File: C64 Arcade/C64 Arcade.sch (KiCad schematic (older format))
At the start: 53 parts, among them J1 Port_1, J10 P2_FIRE3, J11 P1_FIRE1, J12 P1_FIRE2, J13 P1_FIRE3, J14 PWR1, J15 PWR2, J2 Port_2, J3 DIR, J4 UP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

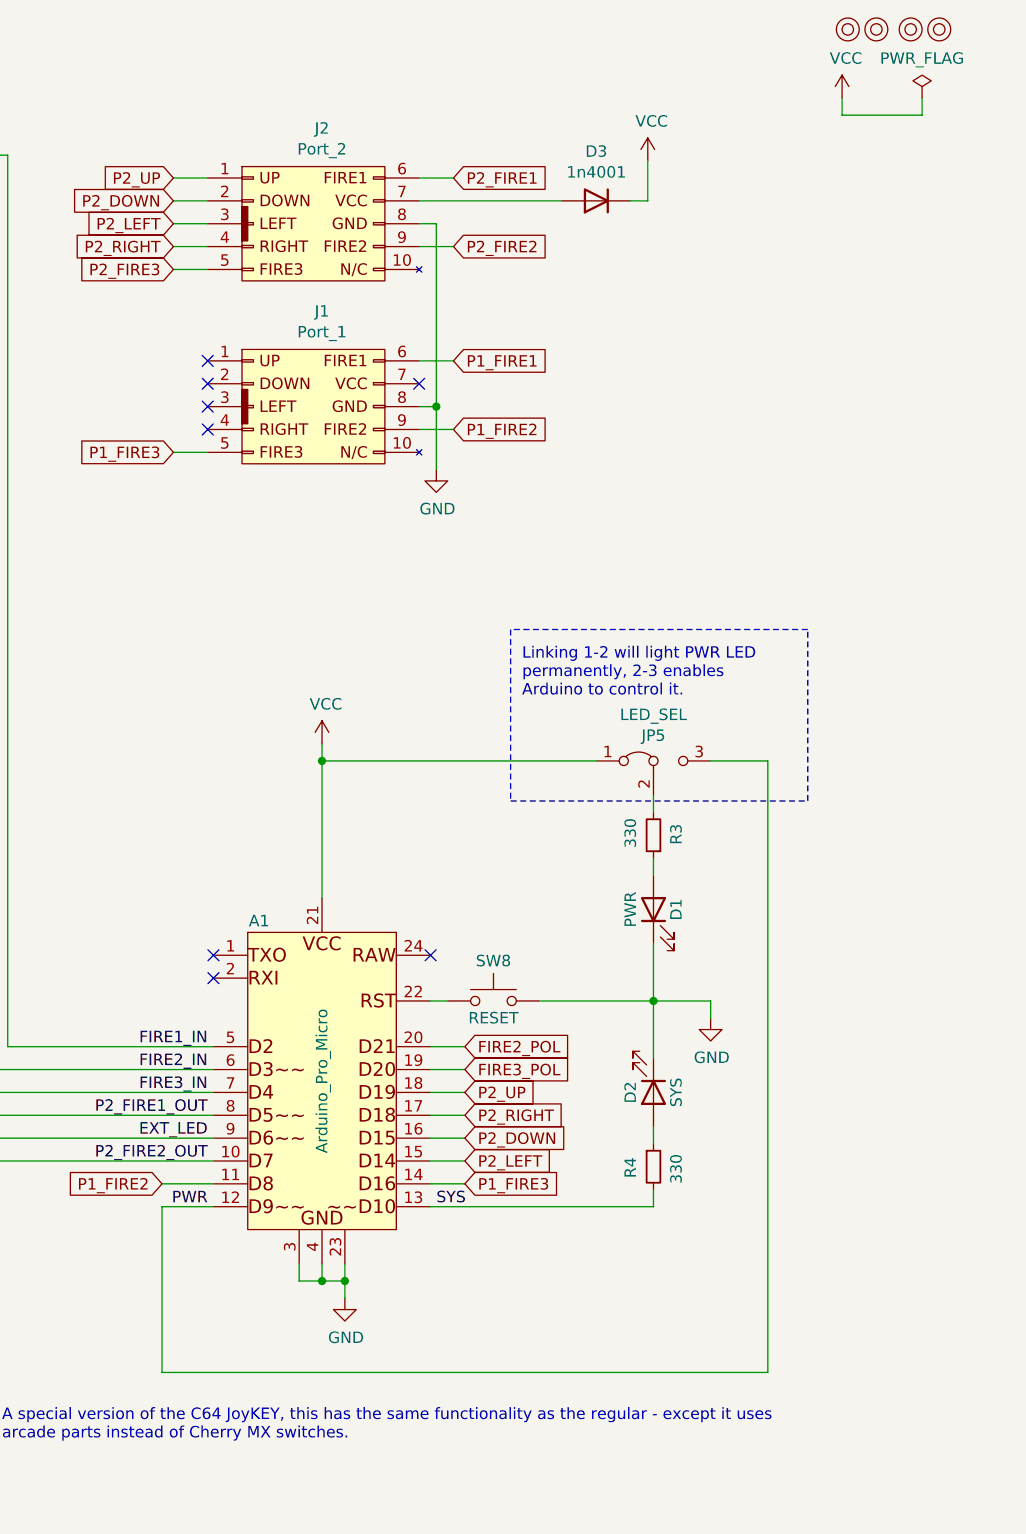
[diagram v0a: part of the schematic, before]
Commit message: Assigned arcade footprints
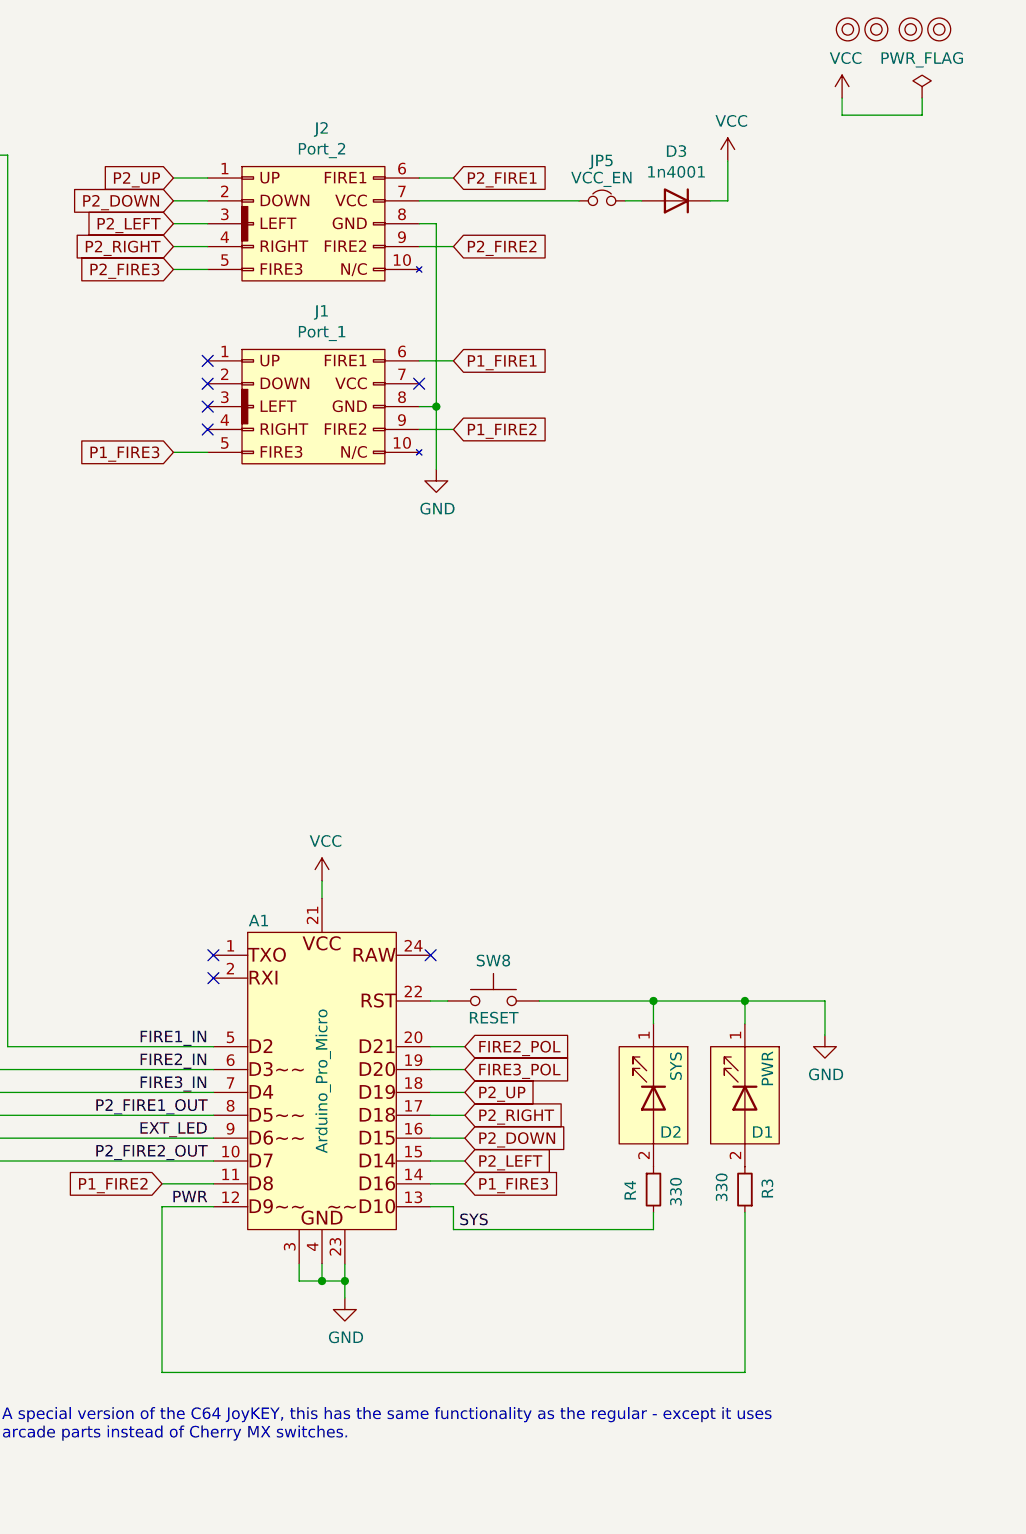
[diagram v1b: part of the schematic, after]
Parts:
- removed D1: PWR, LEDs:LED_D5.0mm, symbol Device:LED
- removed D2: SYS, LEDs:LED_D5.0mm, symbol Device:LED
- removed JP5: LED_SEL, solder_bridge:select, symbol Jumper:Jumper_3_Bridged12
- added D1: PWR, Connector_JST:JST_XH_B2B-XH-A_1x02_P2.50mm_Vertical, symbol arcade:LED_Plugin
- added D2: SYS, Connector_JST:JST_XH_B2B-XH-A_1x02_P2.50mm_Vertical, symbol arcade:LED_Plugin
- added JP5: VCC_EN, Connector_PinHeader_2.54mm:PinHeader_1x02_P2.54mm_Vertical, symbol Device:Jumper_NC_Small
- D10, D5, D6, D7, D8, D9, J10, J11, J12, J13, J14, J15, J4, J5, J6, J7, J8, J9: footprint (none) -> Connector_JST:JST_XH_B2B-XH-A_1x02_P2.50mm_Vertical
- J3: footprint (none) -> Connector_JST:JST_XH_B5B-XH-A_1x05_P2.50mm_Vertical
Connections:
- net GND: now also D1.1 (K), D2.1 (K)
- net PWR: now also R3.1
- net at J2.7 (Pin_7): now also JP5.1; no longer D3.2 (A)
- net at R3.2: now also D1.2 (A)
- net at R4.1: now also D2.2 (A)
- new net: D3.2 (A), JP5.2
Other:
- note removed: "Linking 1-2 will light PWR LED\npermanently, 2-3 enables\nArduino to control it."
- moved on the sheet: D3, R3, R4

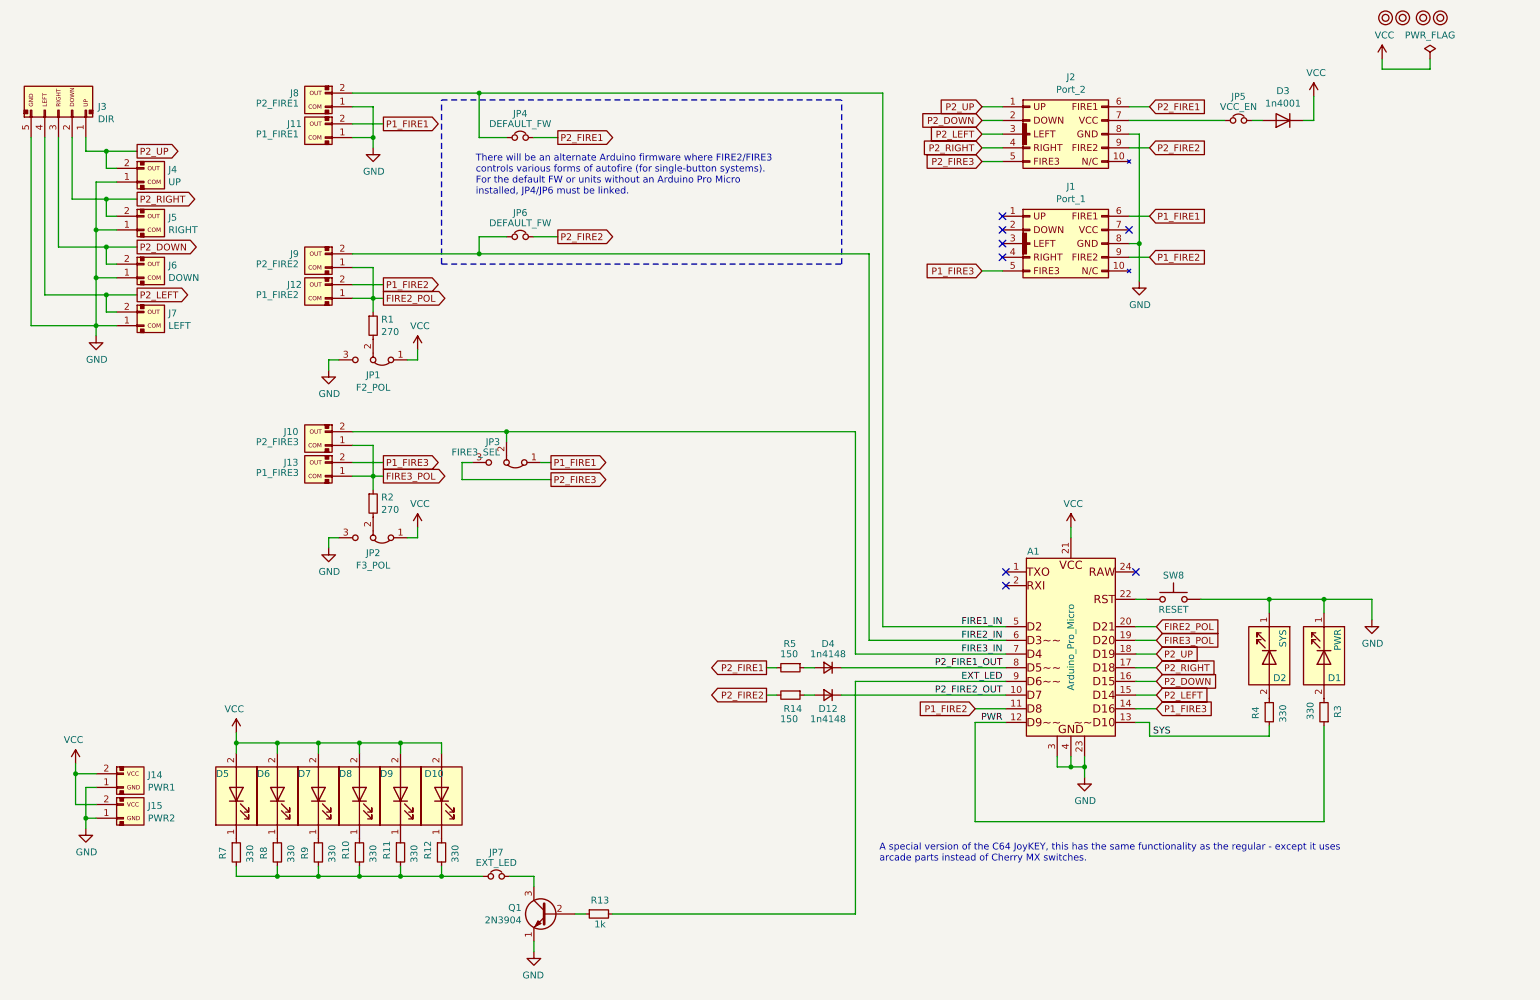
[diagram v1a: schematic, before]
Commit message: Arcade board layout done
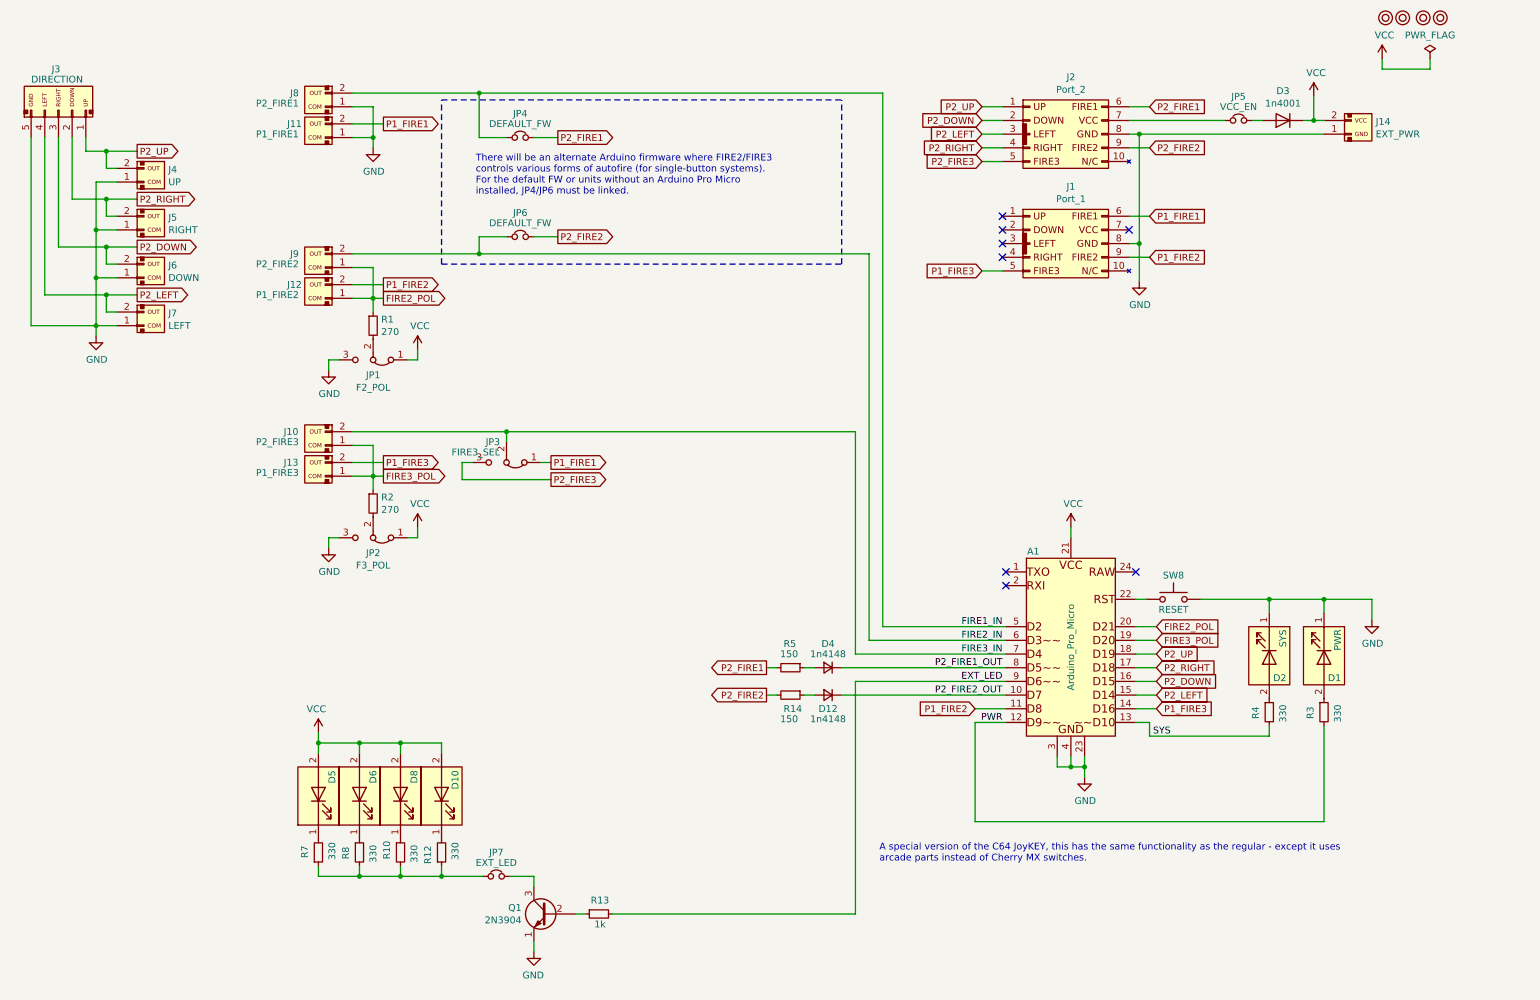
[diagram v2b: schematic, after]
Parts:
- removed D7, D9: LED_Plugin, Connector_JST:JST_XH_B2B-XH-A_1x02_P2.50mm_Vertical, symbol arcade:LED_Plugin
- removed J15: PWR2, Connector_JST:JST_XH_B2B-XH-A_1x02_P2.50mm_Vertical, symbol arcade:PWR
- removed R11, R9: 330, Resistor_THT:R_Axial_DIN0207_L6.3mm_D2.5mm_P10.16mm_Horizontal, symbol Device:R_Small
- J14: value PWR1 -> EXT_PWR
- J3: value DIR -> DIRECTION
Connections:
- net PWR: now also R3.2; no longer R3.1
- net at D1.2 (A): now also R3.1; no longer R3.2
- net at Q1.3 (C): now also JP7.1; no longer JP7.2
- net at D10.1 (K): now also R12.2; no longer R12.1
- net at R7.1: now also JP7.2, R10.2, R12.1, R8.2; no longer D5.1 (K)
- new net: D5.1 (K), R7.2
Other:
- moved on the sheet: D5, D6, D8, J14, R10, R7, R8
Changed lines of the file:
@@
 	3800 6750 3800 6825
 Wire Wire Line
-	3800 6825 3500 6825
-Wire Wire Line
 	3500 6750 3500 6825
-Connection ~ 3500 6825
-Wire Wire Line
-	3500 6825 3200 6825
 Wire Wire Line
 	3200 6750 3200 6825
-Connection ~ 3200 6825
 Wire Wire Line
 	3200 6825 2900 6825
 Wire Wire Line
 	2900 6750 2900 6825
-Connection ~ 2900 6825
-Wire Wire Line
-	2900 6825 2600 6825
-Wire Wire Line
-	2600 6750 2600 6825
-Connection ~ 2600 6825
-Wire Wire Line
-	2600 6825 2300 6825
-Wire Wire Line
-	2300 6750 2300 6825
-Connection ~ 3800 6825
 Wire Wire Line
 	3800 5925 3800 5850
 Wire Wire Line
-	3800 5850 3500 5850
-Wire Wire Line
 	3500 5850 3500 5925
 Wire Wire Line
-	3500 5850 3200 5850
-Wire Wire Line
 	3200 5850 3200 5925
-Connection ~ 3500 5850
 Wire Wire Line
 	3200 5850 2900 5850
 Wire Wire Line
 	2900 5850 2900 5925
-Connection ~ 3200 5850
-Wire Wire Line
-	2900 5850 2600 5850
-Wire Wire Line
-	2600 5850 2600 5925
 Connection ~ 2900 5850
-Wire Wire Line
-	2600 5850 2300 5850
-Wire Wire Line
-	2300 5850 2300 5925
-Connection ~ 2600 5850
-Connection ~ 2300 5850
 $Comp
 L power:VCC #PWR0106
 U 1 1 60023832
-P 2300 5775
-F 0 "#PWR0106" H 2300 5625 50  0001 C CNN
-F 1 "VCC" H 2315 5948 50  0000 C CNN
-F 2 "" H 2300 5775 50  0001 C CNN
-F 3 "" H 2300 5775 50  0001 C CNN
-	1    2300 5775
+P 2900 5775
+F 0 "#PWR0106" H 2900 5625 50  0001 C CNN
+F 1 "VCC" H 2915 5948 50  0000 C CNN
+F 2 "" H 2900 5775 50  0001 C CNN
+F 3 "" H 2900 5775 50  0001 C CNN
+	1    2900 5775
 	-1   0    0    -1
 $EndComp
@@
 L Device:R_Small R7
 U 1 1 6014570E
-P 2300 6650
-F 0 "R7" V 2200 6600 50  0000 L CNN
-F 1 "330" V 2400 6575 50  0000 L CNN
-F 2 "Resistor_THT:R_Axial_DIN0207_L6.3mm_D2.5mm_P10.16mm_Horizontal" H 2300 6650 50  0001 C CNN
-F 3 "~" H 2300 6650 50  0001 C CNN
-	1    2300 6650
-	1    0    0    -1
-$EndComp
-$Comp
-L Device:R_Small R8
-U 1 1 6014BD41
-P 2600 6650
-F 0 "R8" V 2500 6600 50  0000 L CNN
-F 1 "330" V 2700 6575 50  0000 L CNN
-F 2 "Resistor_THT:R_Axial_DIN0207_L6.3mm_D2.5mm_P10.16mm_Horizontal" H 2600 6650 50  0001 C CNN
-F 3 "~" H 2600 6650 50  0001 C CNN
-	1    2600 6650
-	1    0    0    -1
-$EndComp
-$Comp
-L Device:R_Small R9
-U 1 1 6014BD47
 P 2900 6650
-F 0 "R9" V 2800 6600 50  0000 L CNN
+F 0 "R7" V 2800 6600 50  0000 L CNN
 F 1 "330" V 3000 6575 50  0000 L CNN
 F 2 "Resistor_THT:R_Axial_DIN0207_L6.3mm_D2.5mm_P10.16mm_Horizontal" H 2900 6650 50  0001 C CNN
 F 3 "~" H 2900 6650 50  0001 C CNN
 	1    2900 6650
-	1    0    0    -1
-$EndComp
-$Comp
-L Device:R_Small R10
-U 1 1 60152B72
+	1    0    0    1
+$EndComp
+$Comp
+L Device:R_Small R8
+U 1 1 6014BD41
 P 3200 6650
-F 0 "R10" V 3100 6600 50  0000 L CNN
+F 0 "R8" V 3100 6600 50  0000 L CNN
 F 1 "330" V 3300 6575 50  0000 L CNN
 F 2 "Resistor_THT:R_Axial_DIN0207_L6.3mm_D2.5mm_P10.16mm_Horizontal" H 3200 6650 50  0001 C CNN
@@
 $EndComp
 $Comp
-L Device:R_Small R11
-U 1 1 60152B78
+L Device:R_Small R10
+U 1 1 60152B72
 P 3500 6650
-F 0 "R11" V 3400 6600 50  0000 L CNN
+F 0 "R10" V 3400 6600 50  0000 L CNN
 F 1 "330" V 3600 6575 50  0000 L CNN
 F 2 "Resistor_THT:R_Axial_DIN0207_L6.3mm_D2.5mm_P10.16mm_Horizontal" H 3500 6650 50  0001 C CNN
@@
 F 3 "~" H 3800 6650 50  0001 C CNN
 	1    3800 6650
-	1    0    0    -1
+	1    0    0    1
 $EndComp
 Wire Wire Line
@@
 F 3 "~" H 4200 6825 50  0001 C CNN
 	1    4200 6825
-	1    0    0    -1
+	-1   0    0    -1
 $EndComp
 Wire Wire Line
@@
 U 1 1 601F1F84
 P 1000 1225
-F 0 "J3" V 1026 937 50  0000 R CNN
-F 1 "DIR" V 935 937 50  0000 R CNN
+F 0 "J3" V 1300 1275 50  0000 R CNN
+F 1 "DIRECTION" V 1225 1425 50  0000 R CNN
 F 2 "Connector_JST:JST_XH_B5B-XH-A_1x05_P2.50mm_Vertical" H 1000 1225 50  0001 C CNN
 F 3 "~" H 1000 1225 50  0001 C CNN
@@
 U 1 1 6013CF33
 P 3800 6225
-F 0 "D10" V 3950 6350 50  0000 R CNN
+F 0 "D10" H 3975 6125 50  0000 R CNN
 F 1 "LED_Plugin" V 3743 6047 50  0001 R CNN
 F 2 "Connector_JST:JST_XH_B2B-XH-A_1x02_P2.50mm_Vertical" H 3800 6225 50  0001 C CNN
@@
 $EndComp
 $Comp
-L arcade:LED_Plugin D9
-U 1 1 60185272
+L arcade:LED_Plugin D8
+U 1 1 6018EAC5
 P 3500 6225
-F 0 "D9" V 3650 6375 50  0000 R CNN
+F 0 "D8" H 3675 6125 50  0000 R CNN
 F 1 "LED_Plugin" V 3443 6047 50  0001 R CNN
 F 2 "Connector_JST:JST_XH_B2B-XH-A_1x02_P2.50mm_Vertical" H 3500 6225 50  0001 C CNN
@@
 $EndComp
 $Comp
-L arcade:LED_Plugin D8
-U 1 1 6018EAC5
+L arcade:LED_Plugin D6
+U 1 1 601A1981
 P 3200 6225
-F 0 "D8" V 3350 6375 50  0000 R CNN
+F 0 "D6" H 3375 6125 50  0000 R CNN
 F 1 "LED_Plugin" V 3143 6047 50  0001 R CNN
 F 2 "Connector_JST:JST_XH_B2B-XH-A_1x02_P2.50mm_Vertical" H 3200 6225 50  0001 C CNN
@@
 $EndComp
 $Comp
-L arcade:LED_Plugin D7
-U 1 1 60198250
+L arcade:LED_Plugin D5
+U 1 1 601AB1C0
 P 2900 6225
-F 0 "D7" V 3050 6375 50  0000 R CNN
+F 0 "D5" H 3075 6125 50  0000 R CNN
 F 1 "LED_Plugin" V 2843 6047 50  0001 R CNN
 F 2 "Connector_JST:JST_XH_B2B-XH-A_1x02_P2.50mm_Vertical" H 2900 6225 50  0001 C CNN
@@
 $EndComp
 $Comp
-L arcade:LED_Plugin D6
-U 1 1 601A1981
-P 2600 6225
-F 0 "D6" V 2750 6375 50  0000 R CNN
-F 1 "LED_Plugin" V 2543 6047 50  0001 R CNN
-F 2 "Connector_JST:JST_XH_B2B-XH-A_1x02_P2.50mm_Vertical" H 2600 6225 50  0001 C CNN
-F 3 "~" H 2600 6225 50  0001 C CNN
-	1    2600 6225
-	0    -1   -1   0
-$EndComp
-$Comp
-L arcade:LED_Plugin D5
-U 1 1 601AB1C0
-P 2300 6225
-F 0 "D5" V 2450 6375 50  0000 R CNN
-F 1 "LED_Plugin" V 2243 6047 50  0001 R CNN
-F 2 "Connector_JST:JST_XH_B2B-XH-A_1x02_P2.50mm_Vertical" H 2300 6225 50  0001 C CNN
-F 3 "~" H 2300 6225 50  0001 C CNN
-	1    2300 6225
-	0    -1   -1   0
-$EndComp
-$Comp
 L arcade:PWR J14
 U 1 1 601C93F2
-P 1525 6125
-F 0 "J14" H 1653 6166 50  0000 L CNN
-F 1 "PWR1" H 1653 6075 50  0000 L CNN
-F 2 "Connector_JST:JST_XH_B2B-XH-A_1x02_P2.50mm_Vertical" H 1475 6275 50  0001 C CNN
-F 3 "~" H 1475 6275 50  0001 C CNN
-	1    1525 6125
-	1    0    0    -1
-$EndComp
-$Comp
-L arcade:PWR J15
-U 1 1 601CC52A
-P 1525 6350
-F 0 "J15" H 1653 6391 50  0000 L CNN
-F 1 "PWR2" H 1653 6300 50  0000 L CNN
-F 2 "Connector_JST:JST_XH_B2B-XH-A_1x02_P2.50mm_Vertical" H 1475 6500 50  0001 C CNN
-F 3 "~" H 1475 6500 50  0001 C CNN
-	1    1525 6350
-	1    0    0    -1
-$EndComp
-Wire Wire Line
-	1125 6075 1125 6000
-Wire Wire Line
-	1125 6300 1125 6075
-Connection ~ 1125 6075
-Wire Wire Line
-	1125 6075 1275 6075
-Wire Wire Line
-	1125 6300 1275 6300
-Wire Wire Line
-	1275 6175 1200 6175
-Wire Wire Line
-	1200 6175 1200 6400
-Wire Wire Line
-	1200 6400 1275 6400
-Wire Wire Line
-	1200 6400 1200 6475
-Connection ~ 1200 6400
-$Comp
-L power:GND #PWR010
-U 1 1 60227105
-P 1200 6475
-F 0 "#PWR010" H 1200 6225 50  0001 C CNN
-F 1 "GND" H 1205 6302 50  0000 C CNN
-F 2 "" H 1200 6475 50  0001 C CNN
-F 3 "" H 1200 6475 50  0001 C CNN
-	1    1200 6475
-	1    0    0    -1
-$EndComp
-$Comp
-L power:VCC #PWR09
-U 1 1 60231D15
-P 1125 6000
-F 0 "#PWR09" H 1125 5850 50  0001 C CNN
-F 1 "VCC" H 1140 6173 50  0000 C CNN
-F 2 "" H 1125 6000 50  0001 C CNN
-F 3 "" H 1125 6000 50  0001 C CNN
-	1    1125 6000
-	-1   0    0    -1
-$EndComp
-Wire Wire Line
-	2300 5775 2300 5850
+P 10500 1350
+F 0 "J14" H 10628 1391 50  0000 L CNN
+F 1 "EXT_PWR" H 10628 1300 50  0000 L CNN
+F 2 "Connector_JST:JST_XH_B2B-XH-A_1x02_P2.50mm_Vertical" H 10450 1500 50  0001 C CNN
+F 3 "~" H 10450 1500 50  0001 C CNN
+	1    10500 1350
+	1    0    0    -1
+$EndComp
+Wire Wire Line
+	2900 5775 2900 5850
 Text GLabel 7700 5600 0    50   Input ~ 0
 P1_FIRE2
@@
 F 3 "~" H 10250 5625 50  0001 C CNN
 	1    10250 5625
-	-1   0    0    1
+	1    0    0    -1
 $EndComp
 $Comp
@@
 Wire Wire Line
 	8825 1300 9525 1300
+Wire Wire Line
+	3200 6825 3500 6825
+Connection ~ 3200 6825
+Wire Wire Line
+	3500 6825 3800 6825
+Connection ~ 3500 6825
+Connection ~ 3800 6825
+Wire Wire Line
+	3200 5850 3500 5850
+Connection ~ 3200 5850
+Wire Wire Line
+	3500 5850 3800 5850
+Connection ~ 3500 5850
+Wire Wire Line
+	10175 1300 10250 1300
+Connection ~ 10175 1300
+Wire Wire Line
+	8900 1400 10250 1400
+Connection ~ 8900 1400
 $EndSCHEMATC
